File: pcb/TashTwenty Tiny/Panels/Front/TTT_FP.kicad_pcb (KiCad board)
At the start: 2 copper layers, 60 x 22.8 mm, 5 parts

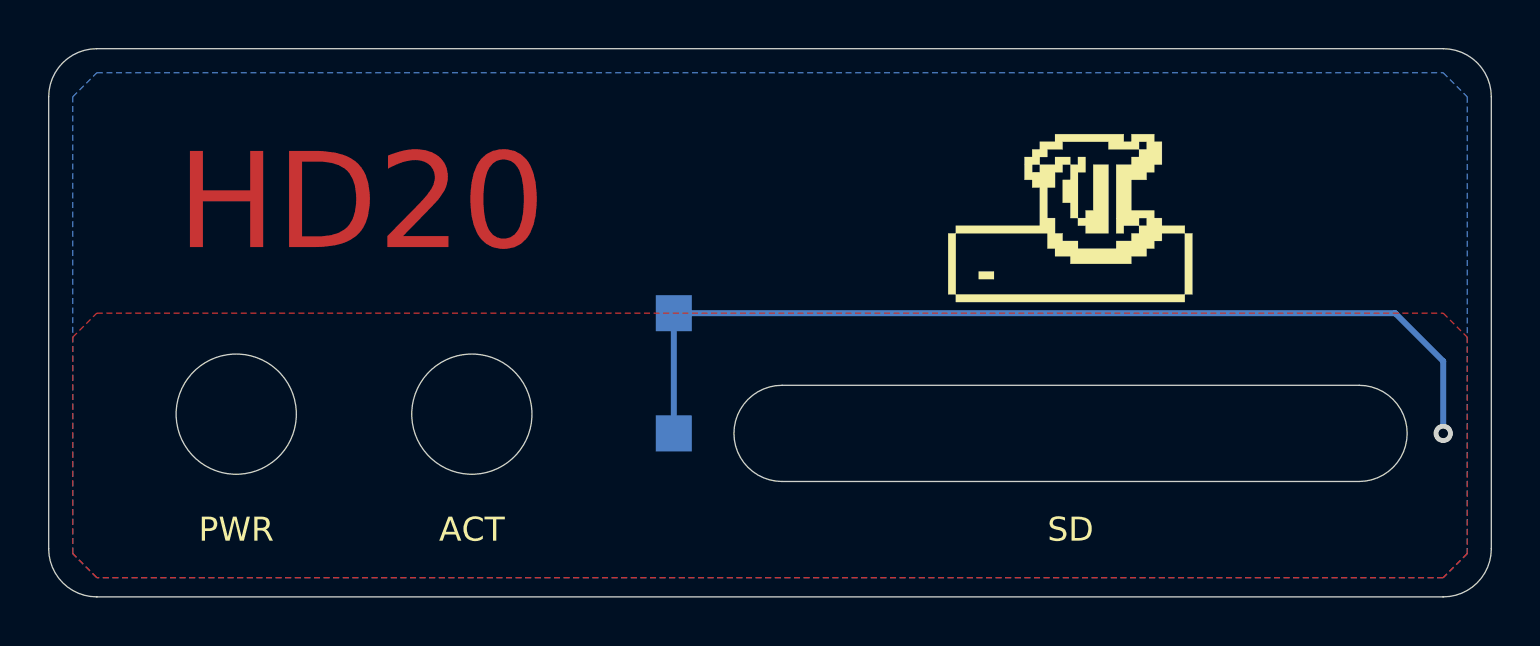
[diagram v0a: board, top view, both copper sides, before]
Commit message: Rev 1.1 Front Panel: align LED and SD holes
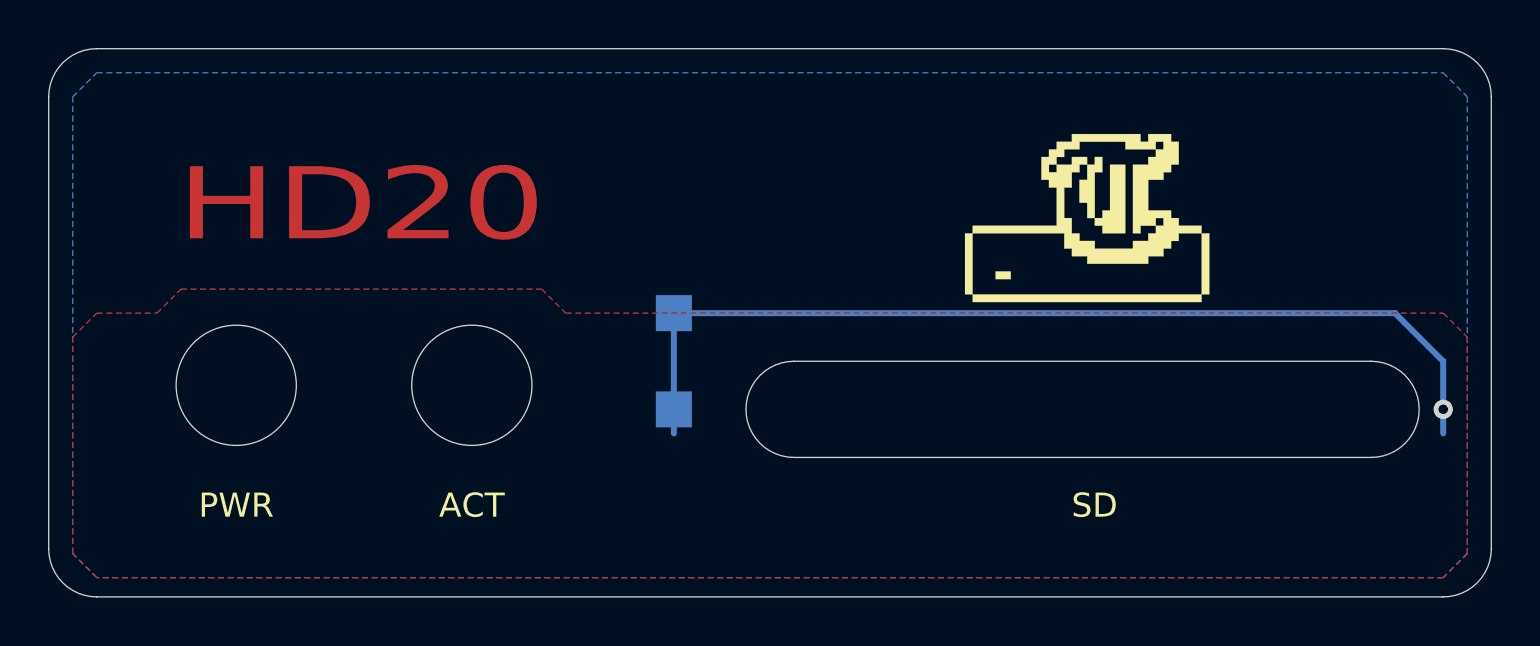
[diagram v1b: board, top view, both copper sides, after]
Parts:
- moved H1 1.20 mm to (45.8, 54.0)
- moved H2 1.20 mm to (55.6, 54.0)
- moved TP1 1.00 mm to (64.0, 55.0)
- moved G*** 0.70 mm to (81.0, 46.6)
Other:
- outline, holes or cut-outs redrawn
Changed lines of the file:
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@@
   (general
     (thickness 1.6)
-    (drawings 17)
+    (drawings 19)
     (tracks 5)
     (zones 0)
@@
   (page A4)
   (title_block
-    (date 2022-03-31)
+    (title "TashTwenty Tiny PCB front panel")
+    (date 2022-06-08)
+    (rev 1.1)
+    (company Lostwave)
+    (comment 1 https://68kmla.org)
+    (comment 2 https://68kmla.org/bb/index.php?threads/tashtwenty-single-chip-dcd-hard-disk-20-interface.39357/)
+    (comment 3 https://github.com/lampmerchant/tashtwenty)
   )
   (layers
     (0 F.Cu signal)
-    (31 B.Cu signal)
+    (31 B.Cu power)
     (36 B.SilkS user)
     (37 F.SilkS user)
@@
     (mod_text_size 1 1)
     (mod_text_width 0.15)
-    (pad_size 1.5 1.5)
-    (pad_drill 0)
+    (pad_size 5 5)
+    (pad_drill 5)
     (pad_to_mask_clearance 0)
     (aux_axis_origin 0 0)
@@
       (effects (font (size 1 1) (thickness 0.15)) (justify mirror))
     )
+    (fp_line (start -0.95 0.95) (end 0.95 0.95) (layer B.SilkS) (width 0.12))
+    (fp_line (start 0.95 0.95) (end 0.95 -0.95) (layer B.SilkS) (width 0.12))
+    (fp_line (start 0.95 -0.95) (end -0.95 -0.95) (layer B.SilkS) (width 0.12))
+    (fp_line (start -0.95 -0.95) (end -0.95 0.95) (layer B.SilkS) (width 0.12))
+    (fp_line (start -1.25 1.25) (end 1.25 1.25) (layer B.CrtYd) (width 0.05))
+    (fp_line (start -1.25 1.25) (end -1.25 -1.25) (layer B.CrtYd) (width 0.05))
+    (fp_line (start 1.25 -1.25) (end 1.25 1.25) (layer B.CrtYd) (width 0.05))
     (fp_line (start 1.25 -1.25) (end -1.25 -1.25) (layer B.CrtYd) (width 0.05))
-    (fp_line (start 1.25 -1.25) (end 1.25 1.25) (layer B.CrtYd) (width 0.05))
-    (fp_line (start -1.25 1.25) (end -1.25 -1.25) (layer B.CrtYd) (width 0.05))
-    (fp_line (start -1.25 1.25) (end 1.25 1.25) (layer B.CrtYd) (width 0.05))
-    (fp_line (start -0.95 -0.95) (end -0.95 0.95) (layer B.SilkS) (width 0.12))
-    (fp_line (start 0.95 -0.95) (end -0.95 -0.95) (layer B.SilkS) (width 0.12))
-    (fp_line (start 0.95 0.95) (end 0.95 -0.95) (layer B.SilkS) (width 0.12))
-    (fp_line (start -0.95 0.95) (end 0.95 0.95) (layer B.SilkS) (width 0.12))
     (fp_text user %R (at 0 1.65) (layer B.Fab)
       (effects (font (size 1 1) (thickness 0.15)) (justify mirror))
@@
   )
   (module TestPoint:TestPoint_Pad_1.5x1.5mm (layer B.Cu)
-    (at 64 56)
+    (at 64 55)
     (descr "SMD rectangular pad as test Point, square 1.5mm side length")
     (tags "test point SMD pad rectangle square")
@@
       (effects (font (size 1 1) (thickness 0.15)) (justify mirror))
     )
+    (fp_line (start -0.95 0.95) (end 0.95 0.95) (layer B.SilkS) (width 0.12))
+    (fp_line (start 0.95 0.95) (end 0.95 -0.95) (layer B.SilkS) (width 0.12))
+    (fp_line (start 0.95 -0.95) (end -0.95 -0.95) (layer B.SilkS) (width 0.12))
+    (fp_line (start -0.95 -0.95) (end -0.95 0.95) (layer B.SilkS) (width 0.12))
+    (fp_line (start -1.25 1.25) (end 1.25 1.25) (layer B.CrtYd) (width 0.05))
+    (fp_line (start -1.25 1.25) (end -1.25 -1.25) (layer B.CrtYd) (width 0.05))
+    (fp_line (start 1.25 -1.25) (end 1.25 1.25) (layer B.CrtYd) (width 0.05))
     (fp_line (start 1.25 -1.25) (end -1.25 -1.25) (layer B.CrtYd) (width 0.05))
-    (fp_line (start 1.25 -1.25) (end 1.25 1.25) (layer B.CrtYd) (width 0.05))
-    (fp_line (start -1.25 1.25) (end -1.25 -1.25) (layer B.CrtYd) (width 0.05))
-    (fp_line (start -1.25 1.25) (end 1.25 1.25) (layer B.CrtYd) (width 0.05))
-    (fp_line (start -0.95 -0.95) (end -0.95 0.95) (layer B.SilkS) (width 0.12))
-    (fp_line (start 0.95 -0.95) (end -0.95 -0.95) (layer B.SilkS) (width 0.12))
-    (fp_line (start 0.95 0.95) (end 0.95 -0.95) (layer B.SilkS) (width 0.12))
-    (fp_line (start -0.95 0.95) (end 0.95 0.95) (layer B.SilkS) (width 0.12))
     (fp_text user %R (at 0 1.65) (layer B.Fab)
       (effects (font (size 1 1) (thickness 0.15)) (justify mirror))
@@
   )
   (module Logo:logo (layer F.Cu)
-    (at 80.3 46.6)
+    (at 81 46.6)
     (fp_text reference G*** (at 0 0) (layer F.SilkS) hide
       (effects (font (size 1.524 1.524) (thickness 0.3)))
@@
       (effects (font (size 1.524 1.524) (thickness 0.3)))
     )
+    (fp_poly (pts (xy 0.8255 -1.4605) (xy 0.508 -1.4605) (xy 0.508 0.4445) (xy 0.1905 0.4445)
+      (xy 0.1905 -0.1905) (xy -0.127 -0.1905) (xy -0.127 -1.143) (xy 0.1905 -1.143)
+      (xy 0.1905 -1.778) (xy 0.508 -1.778) (xy 0.508 -2.0955) (xy 0.8255 -2.0955)
+      (xy 0.8255 -1.4605)) (layer F.SilkS) (width 0.01))
+    (fp_poly (pts (xy 1.778 1.0795) (xy 0.8255 1.0795) (xy 0.8255 0.762) (xy 0.508 0.762)
+      (xy 0.508 0.4445) (xy 0.8255 0.4445) (xy 0.8255 0.127) (xy 1.143 0.127)
+      (xy 1.143 -1.778) (xy 1.778 -1.778) (xy 1.778 1.0795)) (layer F.SilkS) (width 0.01))
+    (fp_poly (pts (xy -2.9845 2.9845) (xy -3.6195 2.9845) (xy -3.6195 2.667) (xy -2.9845 2.667)
+      (xy -2.9845 2.9845)) (layer F.SilkS) (width 0.01))
     (fp_poly (pts (xy 5.2705 1.0795) (xy 5.2705 3.6195) (xy 4.953 3.6195) (xy 4.953 3.937)
       (xy -4.572 3.937) (xy -4.572 3.6195) (xy -4.8895 3.6195) (xy -4.8895 1.0795)
@@
       (xy 4.0005 0.4445) (xy 4.0005 0.762) (xy 4.953 0.762) (xy 4.953 1.0795)
       (xy 5.2705 1.0795)) (layer F.SilkS) (width 0.01))
-    (fp_poly (pts (xy -2.9845 2.9845) (xy -3.6195 2.9845) (xy -3.6195 2.667) (xy -2.9845 2.667)
-      (xy -2.9845 2.9845)) (layer F.SilkS) (width 0.01))
-    (fp_poly (pts (xy 1.778 1.0795) (xy 0.8255 1.0795) (xy 0.8255 0.762) (xy 0.508 0.762)
-      (xy 0.508 0.4445) (xy 0.8255 0.4445) (xy 0.8255 0.127) (xy 1.143 0.127)
-      (xy 1.143 -1.778) (xy 1.778 -1.778) (xy 1.778 1.0795)) (layer F.SilkS) (width 0.01))
-    (fp_poly (pts (xy 0.8255 -1.4605) (xy 0.508 -1.4605) (xy 0.508 0.4445) (xy 0.1905 0.4445)
-      (xy 0.1905 -0.1905) (xy -0.127 -0.1905) (xy -0.127 -1.143) (xy 0.1905 -1.143)
-      (xy 0.1905 -1.778) (xy 0.508 -1.778) (xy 0.508 -2.0955) (xy 0.8255 -2.0955)
-      (xy 0.8255 -1.4605)) (layer F.SilkS) (width 0.01))
   )
   (module MountingHole:MountingHole_5mm (layer F.Cu)
-    (at 55.6 55.2)
+    (at 55.6 54)
     (descr "Mounting Hole 5mm, no annular")
     (tags "mounting hole 5mm no annular")
@@
       (effects (font (size 1 1) (thickness 0.15)))
     )
+    (fp_circle (center 0 0) (end 5.25 0) (layer F.CrtYd) (width 0.05))
     (fp_circle (center 0 0) (end 5 0) (layer Cmts.User) (width 0.15))
-    (fp_circle (center 0 0) (end 5.25 0) (layer F.CrtYd) (width 0.05))
     (fp_text user %R (at 0.3 0) (layer F.Fab)
       (effects (font (size 1 1) (thickness 0.15)))
     )
-    (pad 1 np_thru_hole circle (at 0 0) (size 5 5) (drill 5) (layers *.Cu *.Mask))
+    (pad "" np_thru_hole circle (at 0 0) (size 5 5) (drill 5) (layers *.Cu *.Mask))
   )
   (module MountingHole:MountingHole_5mm (layer F.Cu)
-    (at 45.8 55.2)
+    (at 45.8 54)
     (descr "Mounting Hole 5mm, no annular")
     (tags "mounting hole 5mm no annular")
@@
       (effects (font (size 1 1) (thickness 0.15)))
     )
+    (fp_circle (center 0 0) (end 5.25 0) (layer F.CrtYd) (width 0.05))
     (fp_circle (center 0 0) (end 5 0) (layer Cmts.User) (width 0.15))
-    (fp_circle (center 0 0) (end 5.25 0) (layer F.CrtYd) (width 0.05))
     (fp_text user %R (at 0.3 0) (layer F.Fab)
       (effects (font (size 1 1) (thickness 0.15)))
@@
     (pad 1 np_thru_hole circle (at 0 0) (size 5 5) (drill 5) (layers *.Cu *.Mask))
   )
+  (gr_line (start 37.5 51) (end 35.5 51) (layer Cmts.User) (width 0.15))
+  (gr_line (start 99 51) (end 100.5 51) (layer Cmts.User) (width 0.15))
   (gr_text JLCJLCJLCJLC (at 80.4 60.2) (layer B.SilkS)
     (effects (font (size 1 1) (thickness 0.15)) (justify mirror))
   )
-  (gr_text HD20 (at 51 46.4) (layer F.Cu)
-    (effects (font (size 4 4) (thickness 0.6)))
-  )
-  (gr_text ACT (at 55.6 60) (layer F.SilkS)
+  (gr_text HD20 (at 51 46.5) (layer F.Cu)
+    (effects (font (size 3 4) (thickness 0.6)))
+  )
+  (gr_text ACT (at 55.6 59) (layer F.SilkS)
     (effects (font (size 1 1) (thickness 0.2)))
   )
-  (gr_text PWR (at 45.8 60) (layer F.SilkS)
+  (gr_text PWR (at 45.8 59) (layer F.SilkS)
     (effects (font (size 1 1) (thickness 0.2)))
   )
-  (gr_text SD (at 80.5 60) (layer F.SilkS)
+  (gr_text SD (at 81.5 59) (layer F.SilkS)
     (effects (font (size 1 1) (thickness 0.2)))
   )
-  (gr_arc (start 92.5 56) (end 92.5 58) (angle -180) (layer Edge.Cuts) (width 0.05))
-  (gr_line (start 68.5 58) (end 92.5 58) (layer Edge.Cuts) (width 0.05))
-  (gr_line (start 68.5 54) (end 92.5 54) (layer Edge.Cuts) (width 0.05))
-  (gr_arc (start 68.5 56) (end 68.5 54) (angle -180) (layer Edge.Cuts) (width 0.05))
+  (gr_arc (start 93 55) (end 93 57) (angle -180) (layer Edge.Cuts) (width 0.05))
+  (gr_line (start 69 57) (end 93 57) (layer Edge.Cuts) (width 0.05))
+  (gr_line (start 69 53) (end 93 53) (layer Edge.Cuts) (width 0.05))
+  (gr_arc (start 69 55) (end 69 53) (angle -180) (layer Edge.Cuts) (width 0.05))
   (gr_line (start 40 40) (end 96 40) (layer Edge.Cuts) (width 0.05))
   (gr_line (start 38 60.8) (end 38 42) (layer Edge.Cuts) (width 0.05))
@@
   (segment (start 64 51) (end 94 51) (width 0.25) (layer B.Cu) (net 1))
   (segment (start 94 51) (end 96 53) (width 0.25) (layer B.Cu) (net 1))
-  (via (at 96 56) (size 0.8) (drill 0.4) (layers F.Cu B.Cu) (net 1))
+  (via (at 96 55) (size 0.8) (drill 0.4) (layers F.Cu B.Cu) (net 1))
   (segment (start 96 53) (end 96 56) (width 0.25) (layer B.Cu) (net 1))
   (zone (net 1) (net_name Earth) (layer B.Cu) (hatch edge 0.508)
@@
     (polygon
       (pts
-        (xy 97 52) (xy 97 61) (xy 96 62) (xy 40 62) (xy 39 61)
-        (xy 39 52) (xy 40 51) (xy 96 51)
+        (xy 59.5 51) (xy 96 51) (xy 97 52) (xy 97 61) (xy 96 62)
+        (xy 40 62) (xy 39 61) (xy 39 52) (xy 40 51) (xy 42.5 51)
+        (xy 43.5 50) (xy 58.5 50)
       )
     )
